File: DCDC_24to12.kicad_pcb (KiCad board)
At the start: 4 copper layers, 75 x 74.4 mm, 28 parts, among them J1 Power_IN, J2 Power_OUT, U1 BD9F800MUX-ZE2

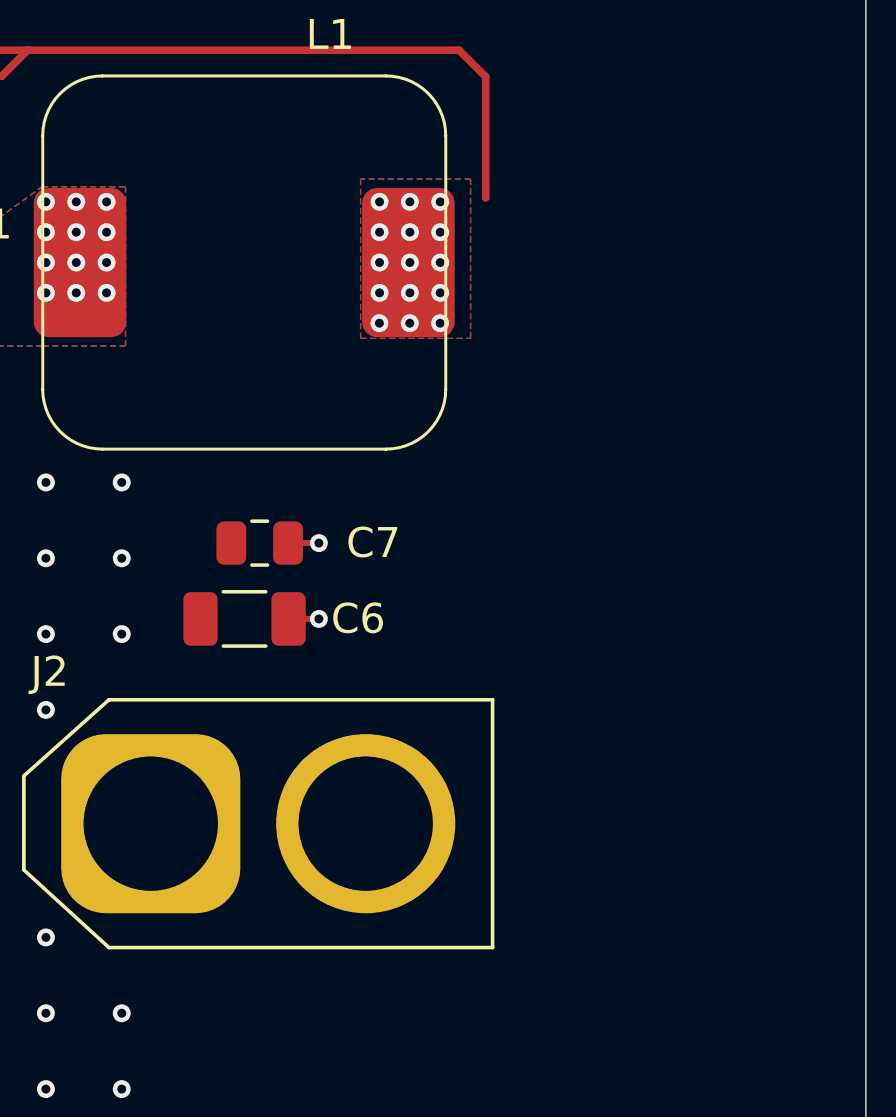
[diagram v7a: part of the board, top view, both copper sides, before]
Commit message: IC直下でGNDとPGNDが直結する問題を解決
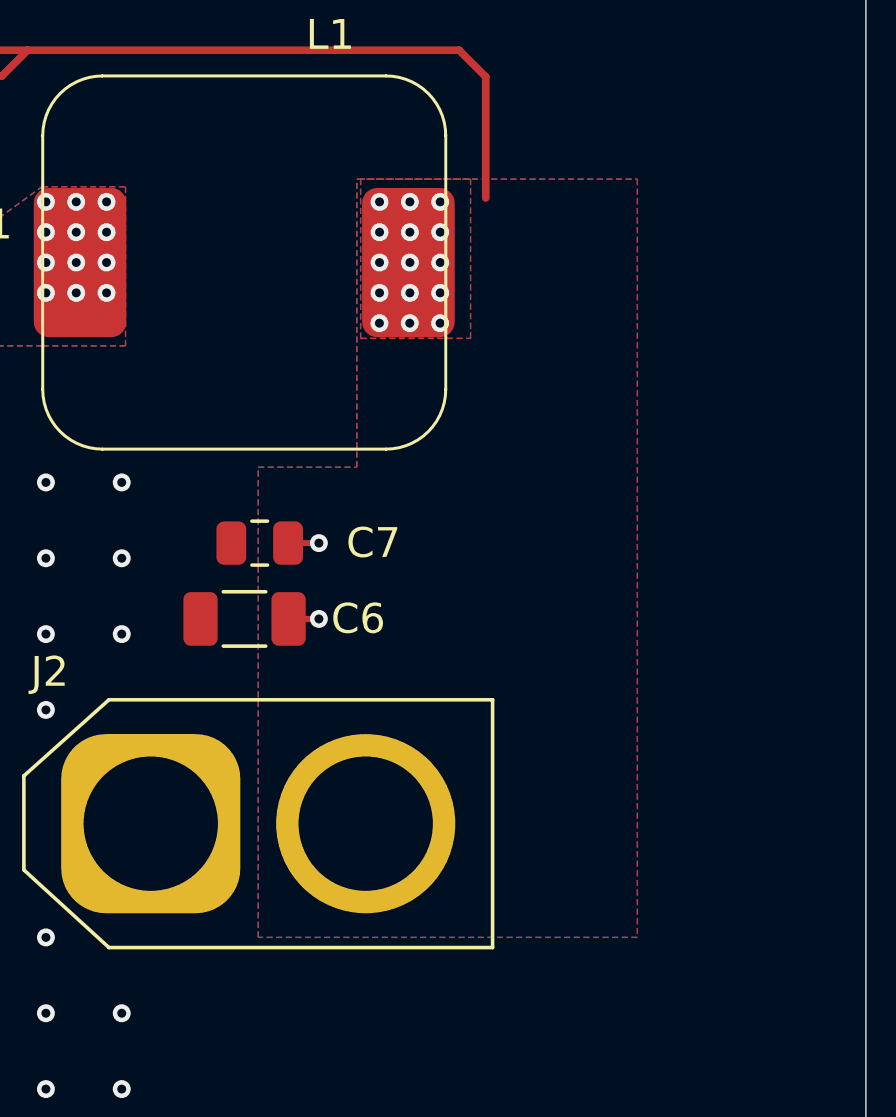
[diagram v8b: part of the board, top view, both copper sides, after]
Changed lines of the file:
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@@
+		(layers "F.Cu" "In1.Cu" "In2.Cu" "B.Cu")
+		(hatch edge 0.5)
+		(connect_pads
+			(clearance 0)
+		)
+		(min_thickness 0.25)
+		(filled_areas_thickness no)
+		(keepout
+			(tracks allowed)
+			(vias allowed)
+			(pads allowed)
+			(copperpour not_allowed)
+			(footprints allowed)
+		)
+		(fill
+			(thermal_gap 0.5)
+			(thermal_bridge_width 1)
+		)
+		(polygon
+			(pts
+				(xy 145.796 93.726) (xy 145.796 96.012) (xy 148.59 96.012) (xy 148.59 93.726)
+			)
+		)
+	)
+	(zone
+		(net 0)
+		(net_name "")
 		(layers "F.Cu" "In1.Cu" "In2.Cu" "B.Cu")
 		(hatch edge 0.5)
@@
 			(pts
 				(xy 153.289 86.106) (xy 153.289 90.17) (xy 168.529 90.17) (xy 168.529 86.106)
+			)
+		)
+	)
+	(zone
+		(net 2)
+		(net_name "+12V")
+		(layers "F.Cu" "In1.Cu" "In2.Cu" "B.Cu")
+		(hatch edge 0.5)
+		(priority 4)
+		(connect_pads
+			(clearance 0.2)
+		)
+		(min_thickness 0.25)
+		(filled_areas_thickness no)
+		(fill yes
+			(thermal_gap 0.5)
+			(thermal_bridge_width 1)
+		)
+		(polygon
+			(pts
+				(xy 161.29 115.57) (xy 161.29 99.822) (xy 164.592 99.822) (xy 164.592 90.17) (xy 173.99 90.17) (xy 173.99 115.57)
 			)
 		)
@@
 			)
 		)
-	)
-	(zone
-		(net 2)
-		(net_name "+12V")
-		(layers "In1.Cu" "In2.Cu")
-		(hatch edge 0.5)
-		(priority 4)
-		(connect_pads
-			(clearance 0.2)
-		)
-		(min_thickness 0.25)
-		(filled_areas_thickness no)
-		(fill yes
-			(thermal_gap 0.5)
-			(thermal_bridge_width 1)
-		)
-		(polygon
-			(pts
-				(xy 161.29 115.57) (xy 161.29 99.822) (xy 164.592 99.822) (xy 164.592 90.17) (xy 173.99 90.17) (xy 173.99 115.57)
-			)
-		)
